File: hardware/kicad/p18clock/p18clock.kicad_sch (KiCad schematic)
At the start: 34 parts, among them J2 Conn_01x05_Pin, J3 USB_C_Receptacle_PowerOnly_6P, J4 Conn_01x04_Pin, U13 LM35-LP, U14 PIC18F2550-ISO, U15 74LS148, Y1 8MHz, Y2 32.768kHz

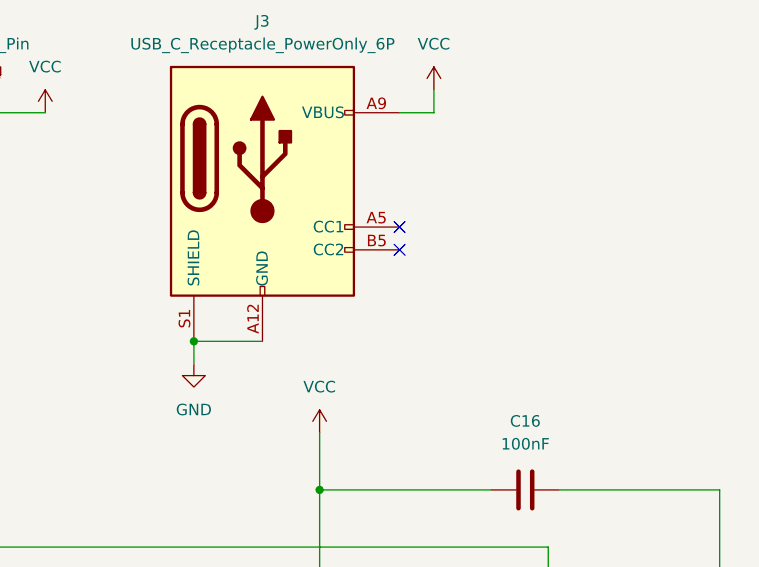
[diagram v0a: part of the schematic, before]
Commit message: [kicad] fix defects in KiCad schematic / PCB
Fix the following defects in KiCad schematic / PCB layout:
- Added 5k1 pull-down resistors in CC1 / CC2 USB-C pins
- Routed LM35.OUT signal on F.Cu layer s.t. it does not split B.Cu
  (GND) fill area
- Added F.Cu (GND) fill area
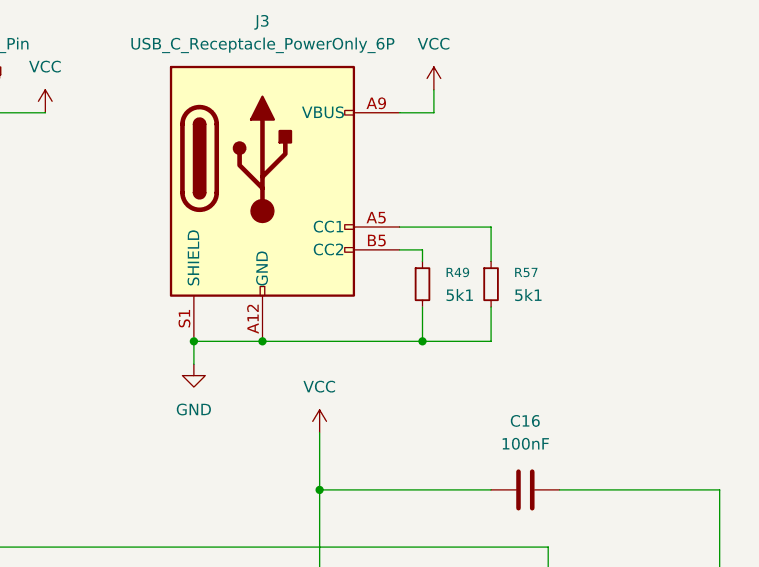
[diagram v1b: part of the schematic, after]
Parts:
- added R49, R57: 5k1, Resistor_SMD:R_0603_1608Metric_Pad0.98x0.95mm_HandSolder, symbol Device:R_Small
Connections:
- net GND: now also R49.2, R57.2
- net at J3.A5 (CC1): now also R57.1
- net at J3.B5 (CC2): now also R49.1
- no-connect marks 13 -> 11
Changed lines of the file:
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@@
 	)
 	(junction
+		(at 223.52 49.53)
+		(diameter 0)
+		(color 0 0 0 0)
+	)
+	(junction
 		(at 170.18 38.1)
 		(diameter 0)
@@
 	)
 	(junction
+		(at 241.3 49.53)
+		(diameter 0)
+		(color 0 0 0 0)
+	)
+	(junction
 		(at 119.38 58.42)
 		(diameter 0)
@@
 	)
 	(no_connect
-		(at 238.76 39.37)
-	)
-	(no_connect
 		(at 157.48 132.08)
 	)
 	(no_connect
-		(at 238.76 36.83)
-	)
-	(no_connect
 		(at 257.81 80.01)
 	)
@@
 	(wire
 		(pts
+			(xy 241.3 39.37) (xy 241.3 40.64)
+		)
+		(stroke
+			(width 0)
+			(type default)
+		)
+	)
+	(wire
+		(pts
 			(xy 137.16 35.56) (xy 137.16 24.13)
 		)
@@
 	(wire
 		(pts
+			(xy 238.76 39.37) (xy 241.3 39.37)
+		)
+		(stroke
+			(width 0)
+			(type default)
+		)
+	)
+	(wire
+		(pts
 			(xy 247.65 133.35) (xy 247.65 151.13)
 		)
@@
 	(wire
 		(pts
+			(xy 238.76 36.83) (xy 248.92 36.83)
+		)
+		(stroke
+			(width 0)
+			(type default)
+		)
+	)
+	(wire
+		(pts
 			(xy 245.11 105.41) (xy 245.11 124.46)
 		)
@@
 	(wire
 		(pts
+			(xy 248.92 36.83) (xy 248.92 40.64)
+		)
+		(stroke
+			(width 0)
+			(type default)
+		)
+	)
+	(wire
+		(pts
 			(xy 113.03 21.59) (xy 113.03 27.94)
 		)
@@
 	(wire
 		(pts
+			(xy 241.3 45.72) (xy 241.3 49.53)
+		)
+		(stroke
+			(width 0)
+			(type default)
+		)
+	)
+	(wire
+		(pts
 			(xy 127 49.53) (xy 127 50.8)
 		)
@@
 	(wire
 		(pts
+			(xy 248.92 49.53) (xy 241.3 49.53)
+		)
+		(stroke
+			(width 0)
+			(type default)
+		)
+	)
+	(wire
+		(pts
 			(xy 274.32 92.71) (xy 274.32 66.04)
 		)
@@
 	(wire
 		(pts
+			(xy 241.3 49.53) (xy 223.52 49.53)
+		)
+		(stroke
+			(width 0)
+			(type default)
+		)
+	)
+	(wire
+		(pts
 			(xy 139.7 181.61) (xy 113.03 181.61)
 		)
@@
 	(wire
 		(pts
+			(xy 248.92 45.72) (xy 248.92 49.53)
+		)
+		(stroke
+			(width 0)
+			(type default)
+		)
+	)
+	(wire
+		(pts
 			(xy 144.78 138.43) (xy 187.96 138.43)
 		)
@@
 	)
 	(symbol
+		(lib_id "Device:R_Small")
+		(at 241.3 43.18 0)
+		(unit 1)
+		(exclude_from_sim no)
+		(in_bom yes)
+		(on_board yes)
+		(dnp no)
+		(fields_autoplaced yes)
+		(property "Reference" "R49"
+			(at 243.84 41.9099 0)
+			(effects
+				(font
+					(size 1.016 1.016)
+				)
+				(justify left)
+			)
+		)
+		(property "Value" "5k1"
+			(at 243.84 44.4499 0)
+			(effects
+				(font
+					(size 1.27 1.27)
+				)
+				(justify left)
+			)
+		)
+		(property "Footprint" "Resistor_SMD:R_0603_1608Metric_Pad0.98x0.95mm_HandSolder"
+			(at 241.3 43.18 0)
+			(effects
+				(font
+					(size 1.27 1.27)
+				)
+				(hide yes)
+			)
+		)
+		(property "Datasheet" "~"
+			(at 241.3 43.18 0)
+			(effects
+				(font
+					(size 1.27 1.27)
+				)
+				(hide yes)
+			)
+		)
+		(property "Description" "Resistor, small symbol"
+			(at 241.3 43.18 0)
+			(effects
+				(font
+					(size 1.27 1.27)
+				)
+				(hide yes)
+			)
+		)
+		(pin "2"
+		)
+		(pin "1"
+		)
+		(instances
+			(project ""
+				(path "/43c2438d-d6fa-45f8-b47d-7d2793ca06b3"
+					(reference "R49")
+					(unit 1)
+				)
+			)
+		)
+	)
+	(symbol
 		(lib_id "Diode:1N4148")
 		(at 163.83 58.42 270)
@@
 					(unit 1)
 				)
+			)
+		)
+	)
+	(symbol
+		(lib_id "Device:R_Small")
+		(at 248.92 43.18 0)
+		(unit 1)
+		(exclude_from_sim no)
+		(in_bom yes)
+		(on_board yes)
+		(dnp no)
+		(fields_autoplaced yes)
+		(property "Reference" "R57"
+			(at 251.46 41.9099 0)
+			(effects
+				(font
+					(size 1.016 1.016)
+				)
+				(justify left)
+			)
+		)
+		(property "Value" "5k1"
+			(at 251.46 44.4499 0)
+			(effects
+				(font
+					(size 1.27 1.27)
+				)
+				(justify left)
+			)
+		)
+		(property "Footprint" "Resistor_SMD:R_0603_1608Metric_Pad0.98x0.95mm_HandSolder"
+			(at 248.92 43.18 0)
+			(effects
+				(font
+					(size 1.27 1.27)
+				)
+				(hide yes)
+			)
+		)
+		(property "Datasheet" "~"
+			(at 248.92 43.18 0)
+			(effects
+				(font
+					(size 1.27 1.27)
+				)
+				(hide yes)
+			)
+		)
+		(property "Description" "Resistor, small symbol"
+			(at 248.92 43.18 0)
+			(effects
+				(font
+					(size 1.27 1.27)
+				)
+				(hide yes)
+			)
+		)
+		(pin "2"
+		)
+		(pin "1"
+		)
+		(instances
+			(project ""
+				(path "/43c2438d-d6fa-45f8-b47d-7d2793ca06b3"
+					(reference "R57")
+					(unit 1)
+				)

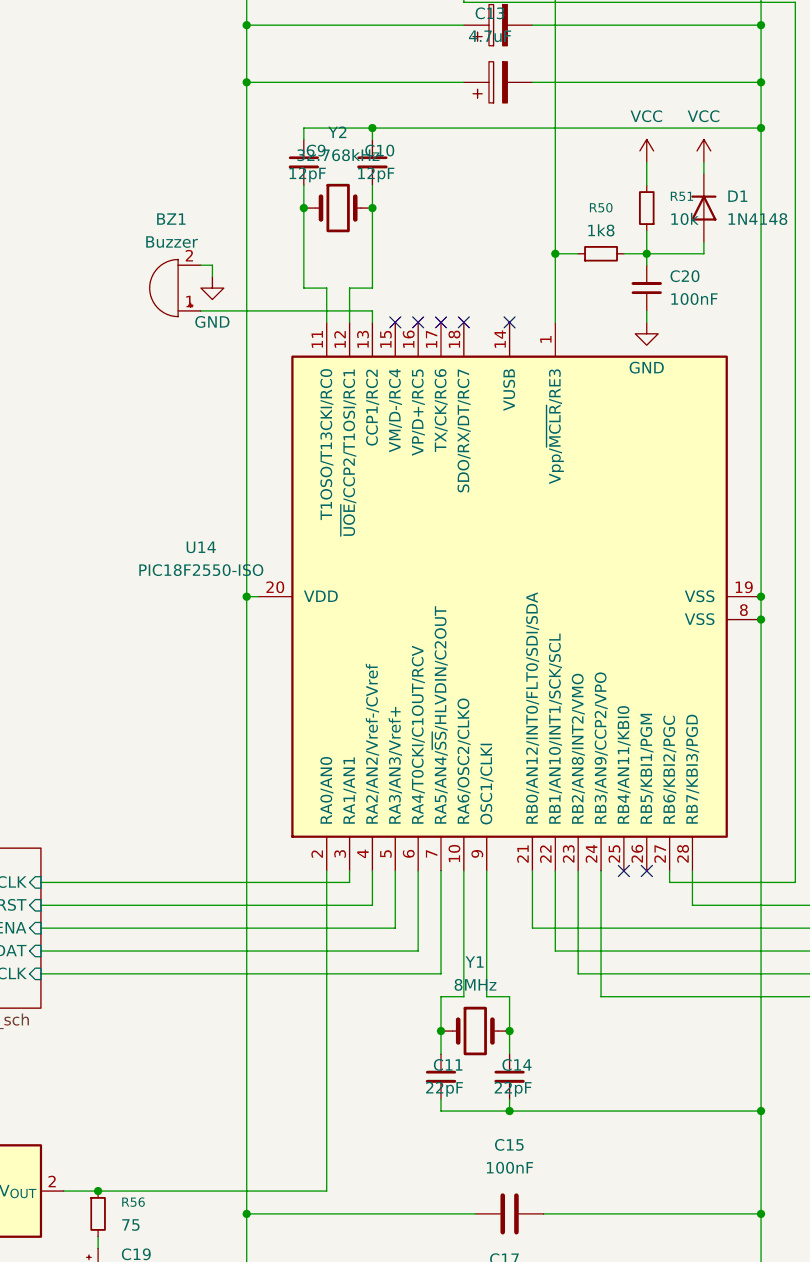
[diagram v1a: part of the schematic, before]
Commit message: [hardware] Fix errata in XTAL capacitor values
Swap XTAL capacitors (8MHz should be 12-15pF; 32.768kHz should be
20-22pF).

Closes #23.
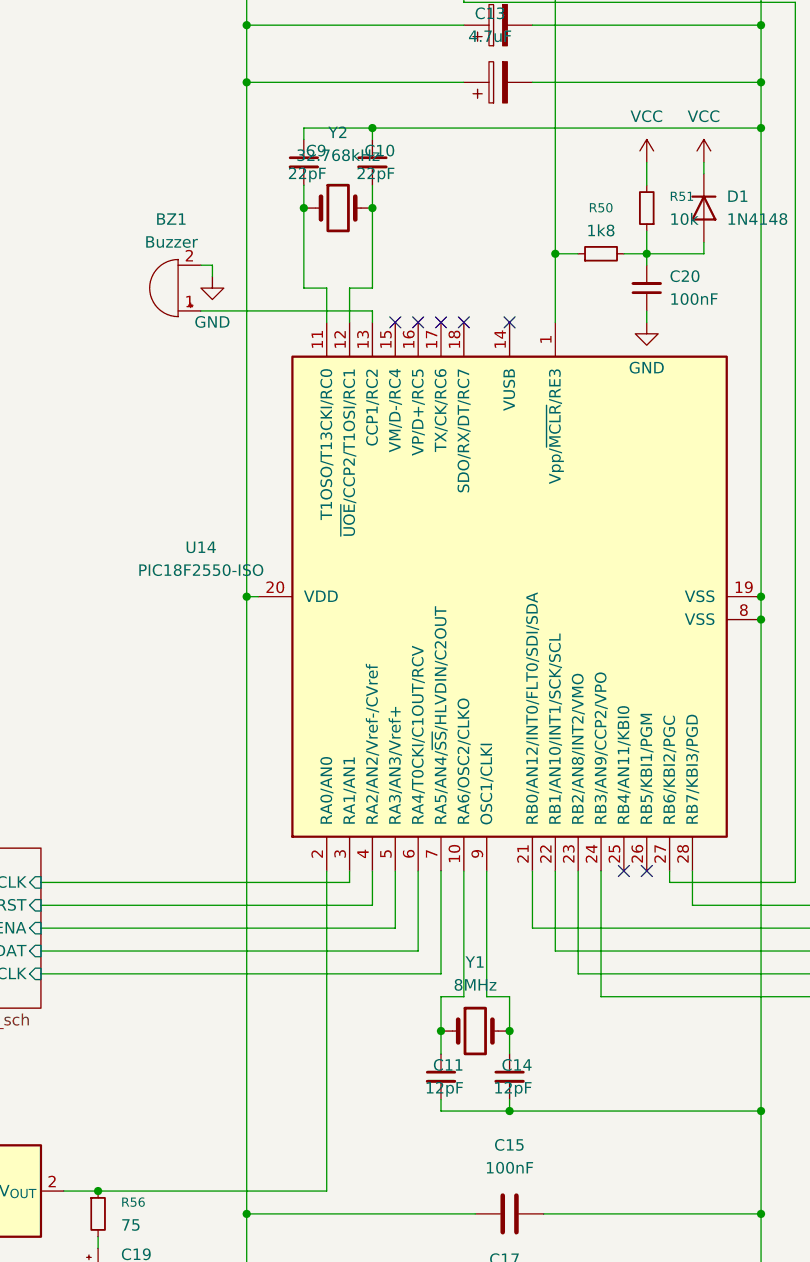
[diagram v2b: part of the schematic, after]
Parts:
- C10, C9: value 12pF -> 22pF
- C11, C14: value 22pF -> 12pF
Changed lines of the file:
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@@
 			)
 		)
-		(property "Value" "12pF"
+		(property "Value" "22pF"
 			(at 121.92 54.6162 0)
 			(effects
@@
 			)
 		)
-		(property "Value" "22pF"
+		(property "Value" "12pF"
 			(at 137.16 156.2162 0)
 			(effects
@@
 			)
 		)
-		(property "Value" "22pF"
+		(property "Value" "12pF"
 			(at 144.78 156.2162 0)
 			(effects
@@
 			)
 		)
-		(property "Value" "12pF"
+		(property "Value" "22pF"
 			(at 129.54 54.6162 0)
 			(effects
